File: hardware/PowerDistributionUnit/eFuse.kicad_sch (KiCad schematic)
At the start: 6 parts, among them U1 TPS25983

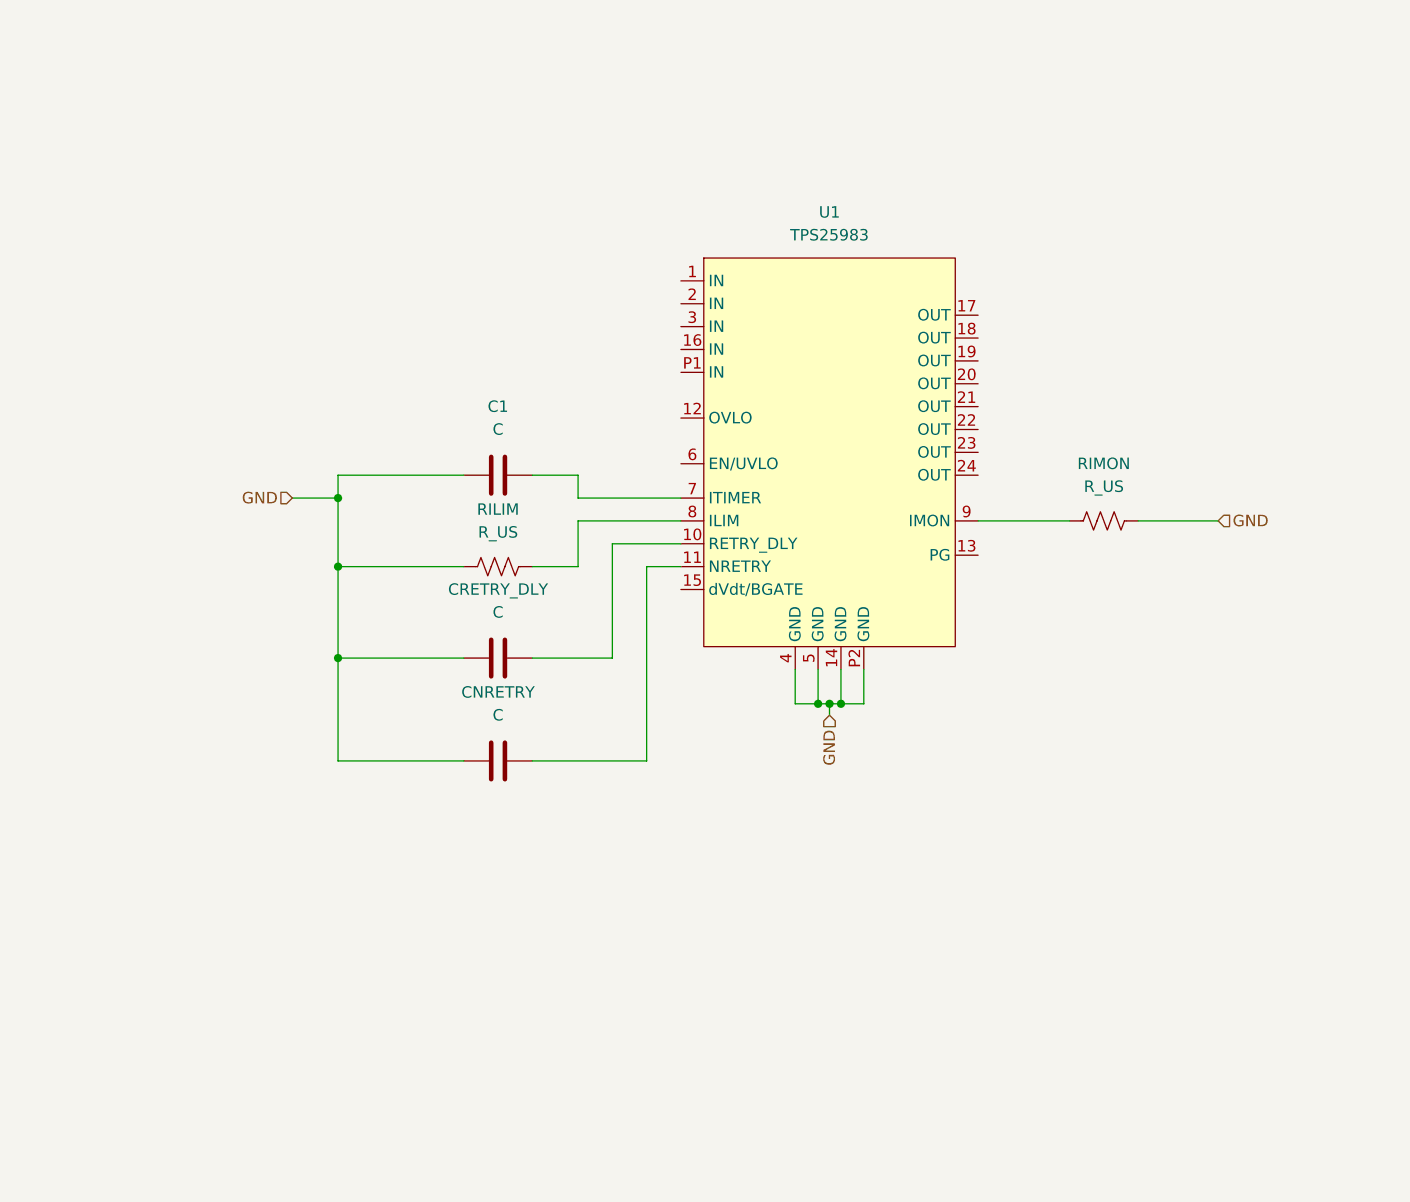
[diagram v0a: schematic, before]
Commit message: Added components on eFuse sheet
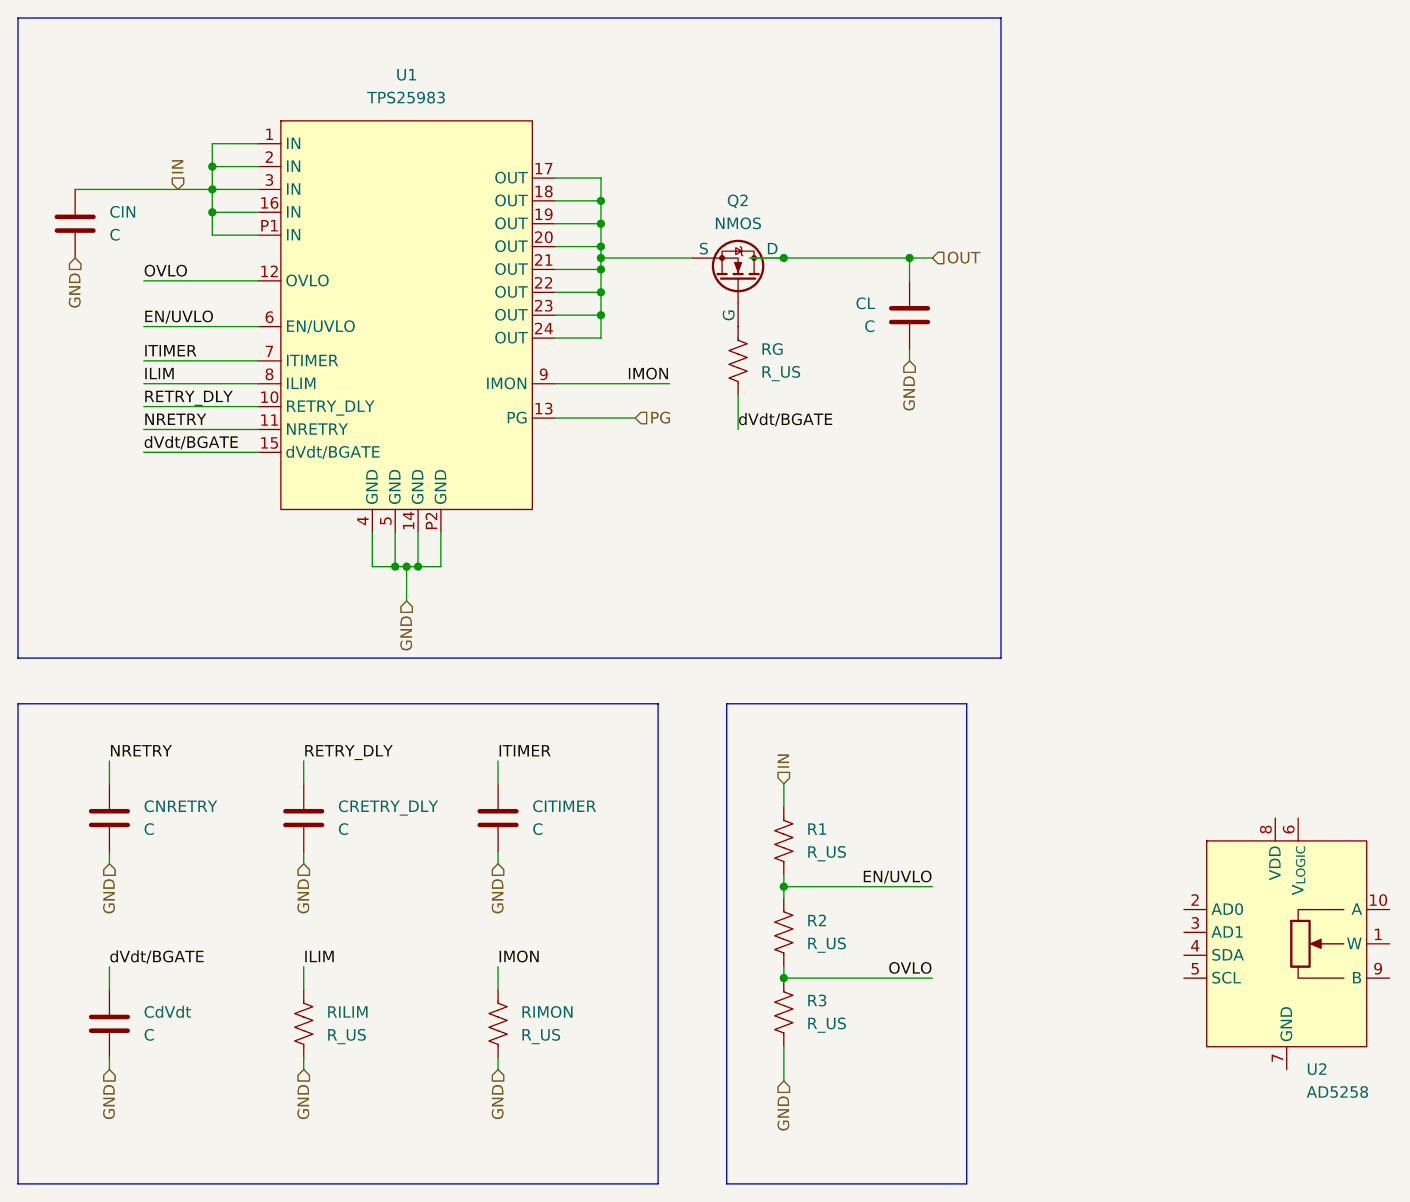
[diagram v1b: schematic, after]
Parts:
- removed C1: C, symbol Device:C
- added CIN, CITIMER, CL, CdVdt: C, symbol Device:C
- added Q2: NMOS, symbol Simulation_SPICE:NMOS
- added R1, R2, R3, RG: R_US, symbol Device:R_US
- added U2: AD5258, symbol PowerDistributionUnitLib:AD5258
- renumbered CRETRY_DLY to CNRETRY, CNRETRY to CRETRY_DLY
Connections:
- net GND: now also RIMON.1, CIN.2, CITIMER.1, CL.2, CdVdt.2, R3.2; no longer RIMON.2
- net IMON: now reaches U1.9 (IMON)
- net IMON: now also RIMON.2; no longer RIMON.1
- net NRETRY: now reaches U1.11 (NRETRY)
- net NRETRY: now also CNRETRY.2; no longer CRETRY_DLY.2
- net RETRY_DLY: now reaches U1.10 (RETRY_DLY)
- net RETRY_DLY: now also CRETRY_DLY.2; no longer CNRETRY.2
- net IN: now reaches U1.1 (IN)
- net IN: now also U1.16 (IN), U1.2 (IN), U1.3 (IN), U1.P1 (IN), CIN.1, R1.1
- net OVLO: now reaches U1.12 (OVLO)
- net OVLO: now also R2.2, R3.1
- net PG: now reaches U1.13 (PG)
- net dVdt/BGATE: now reaches U1.15 (dVdt/BGATE)
- net dVdt/BGATE: now also CdVdt.1, RG.2
- net at U1.17 (OUT): now also U1.18 (OUT), U1.19 (OUT), U1.20 (OUT), U1.21 (OUT), U1.22 (OUT), U1.23 (OUT), U1.24 (OUT), Q2.3 (S)
- net EN/UVLO: now reaches U1.6 (EN/UVLO)
- net EN/UVLO: now also R1.2, R2.1
- net ITIMER: now reaches U1.7 (ITIMER)
- net ITIMER: now also CITIMER.2
- net ILIM: now reaches RILIM.2, U1.8 (ILIM)
- new net: Q2.2 (G), RG.1
- new net OUT: CL.1, Q2.1 (D)
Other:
- moved on the sheet: CNRETRY, CRETRY_DLY, RILIM, U1

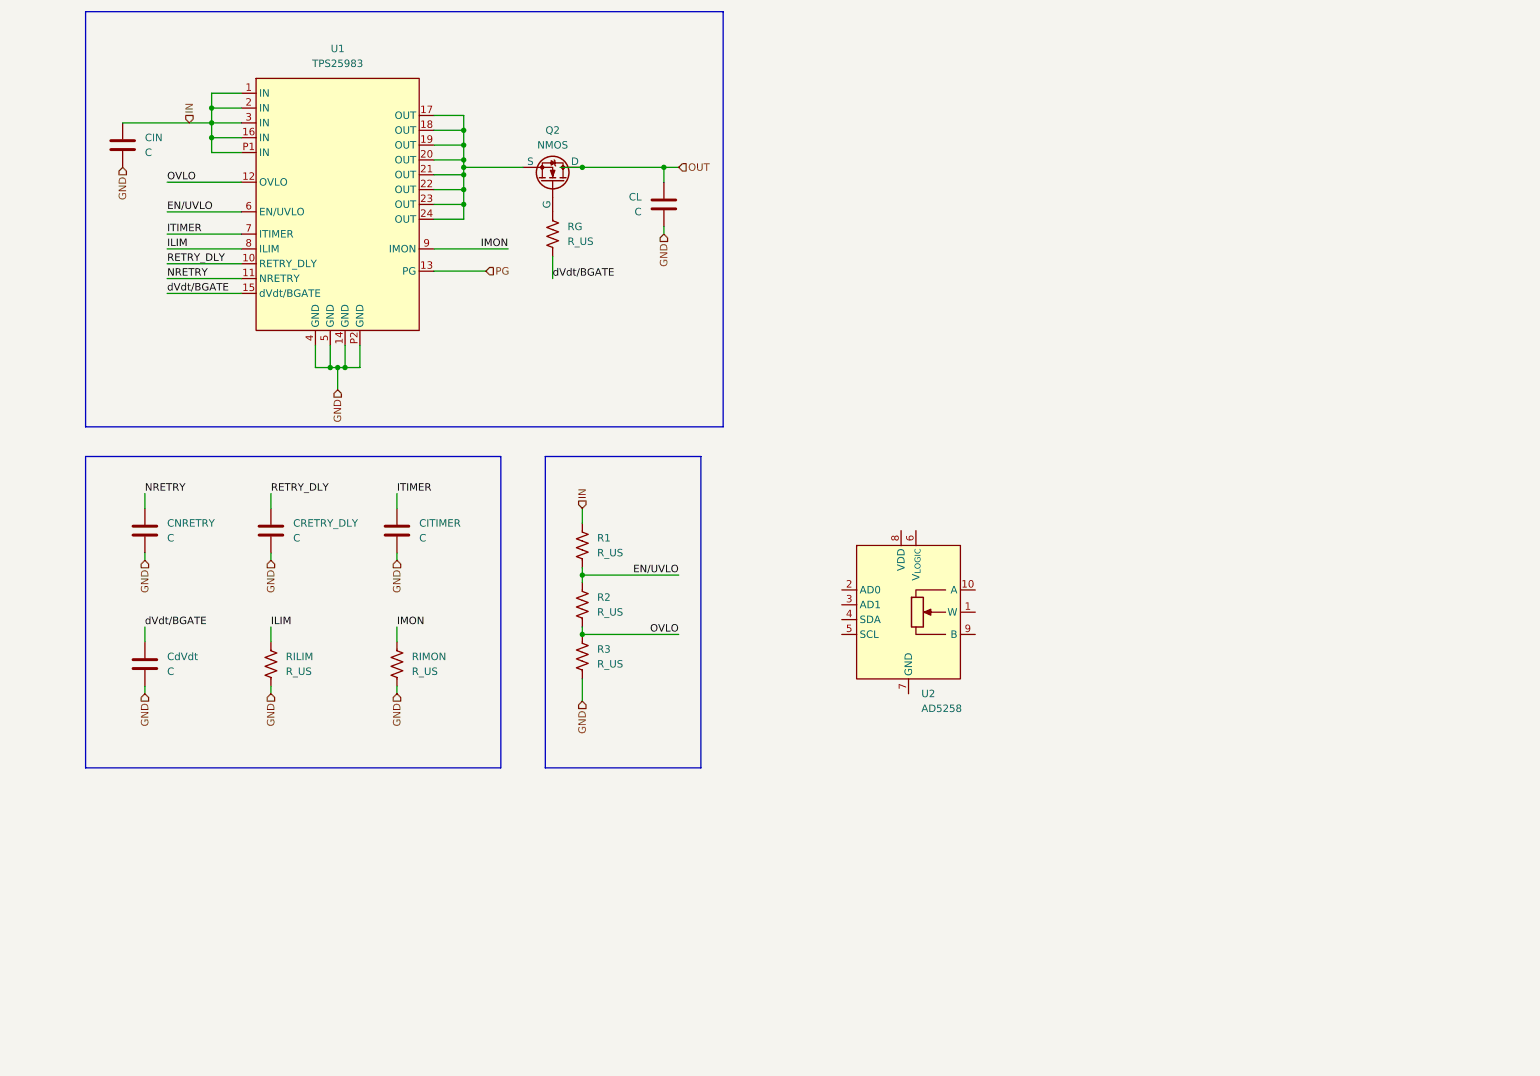
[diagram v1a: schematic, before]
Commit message: aesthetic updates (wire colors, slimmed digital pot symbol), added slight documentation on eFuse retries to schematic, prepared for digital pot wiring a bit, other fun stuff
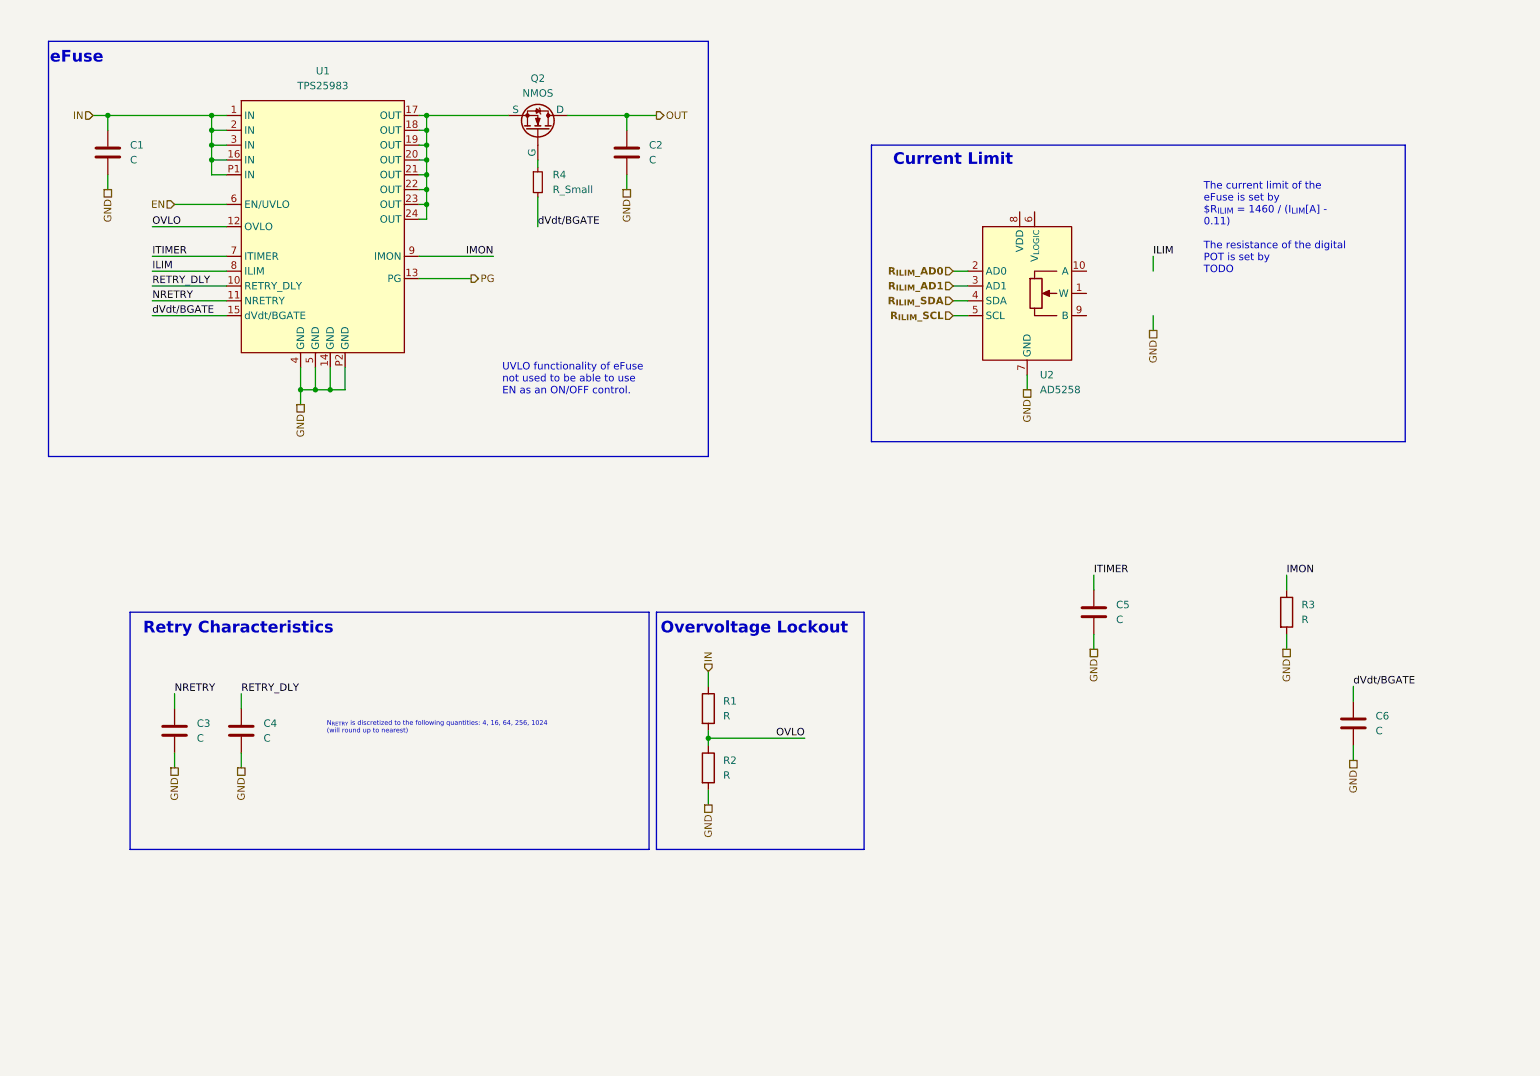
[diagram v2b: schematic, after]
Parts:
- removed CIN, CITIMER, CL, CNRETRY, CRETRY_DLY, CdVdt: C, symbol Device:C
- removed R1, R2, R3, RG, RILIM, RIMON: R_US, symbol Device:R_US
- added C1, C2, C3, C4, C5, C6: C, symbol Device:C
- added R1, R2, R3: R, symbol Device:R
- added R4: R_Small, symbol Device:R_Small
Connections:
- net GND: now also U2.7 (GND), C1.2, C2.2, C3.2, C4.2, C5.2, C6.2, R2.2, R3.2
- net IMON: now also R3.1
- net IN: now also C1.1, R1.1
- net ITIMER: now also C5.1
- net NRETRY: now also C3.1
- net OUT: now also C2.1
- net OVLO: now also R1.2, R2.1
- net RETRY_DLY: now also C4.1
- net dVdt/BGATE: now also C6.1, R4.2
- net at Q2.2 (G): now also R4.1
- net R_{ILIM}_AD0: now reaches U2.2 (AD0)
- net R_{ILIM}_AD1: now reaches U2.3 (AD1)
- net R_{ILIM}_SDA: now reaches U2.4 (SDA)
- net R_{ILIM}_SCL: now reaches U2.5 (SCL)
- net EN/UVLO renamed EN
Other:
- note added: "Current Limit"
- note added: "Overvoltage Lockout"
- note added: "Retry Characteristics"
- note added: "UVLO functionality of eFuse not used to be able to use EN as an ON/OFF control."
- note added: "eFuse"
- moved on the sheet: Q2, U1, U2

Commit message: Gave components values
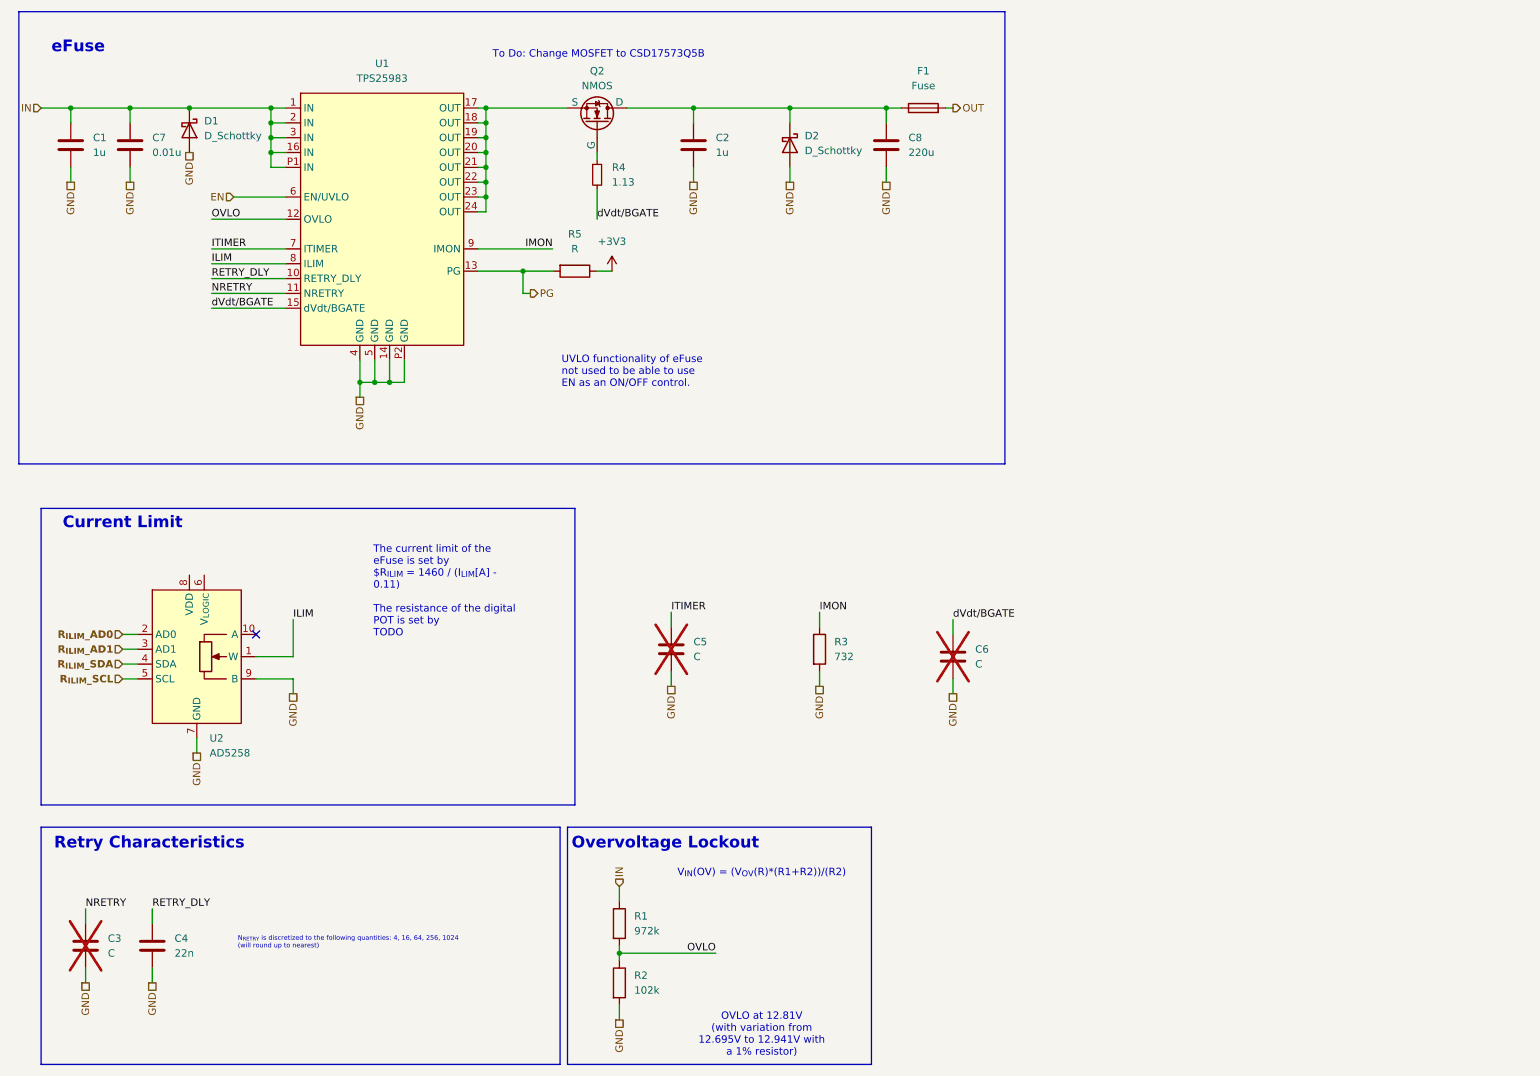
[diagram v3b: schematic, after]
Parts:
- added C7: 0.01u, symbol Device:C
- added C8: 220u, symbol Device:C
- added D1, D2: D_Schottky, symbol Device:D_Schottky
- added F1: Fuse, symbol Device:Fuse
- added R5: R, symbol Device:R
- C1, C2: value C -> 1u
- C3, C5, C6: now not fitted
- C4: value C -> 22n
- R1: value R -> 972k
- R2: value R -> 102k
- R3: value R -> 732
- R4: value R_Small -> 1.13
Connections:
- net GND: now also U2.9 (B), C7.2, C8.2, D1.2 (A), D2.2 (A)
- net ILIM: now also U2.1 (W)
- net IN: now also C7.1, D1.1 (K)
- net OUT: now also F1.2; no longer C2.1, Q2.1 (D)
- net PG: now also R5.2
- new net: C2.1, C8.1, D2.1 (K), F1.1, Q2.1 (D)
- new net +3V3: R5.1
- no-connect marks 0 -> 1
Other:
- note added: "OVLO at 12.81V (with variation from 12.695V to 12.941V with a 1% resistor)"
- note added: "To Do: Change MOSFET to CSD17573Q5B"
- note added: "V_{IN}(OV) = (V_{OV}(R)*(R1+R2))/(R2)"
- moved on the sheet: C1, C2, C4, Q2, R1, R2, R3, R4, U1, U2
